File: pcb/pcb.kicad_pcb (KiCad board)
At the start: 6 copper layers, 172 parts, among them J1 mcu_debug, J1201 Conn_02x07_Top_Bottom, J1401 FPGA_JTAG, J301 Conn_02x05_Top_Bottom, J302 1658525-9, J601 DB15_Female_HighDensity, U201 TPS54325PWPR, U202 TPS54294PWP, U301 BGA112, U401 COM-09032, U666 XC7A75T-FTG256, U701 AS7C316098A-10TIN, Y1101 ECS-2520MV-080-BN-TR, Y301 Crystal_GND24

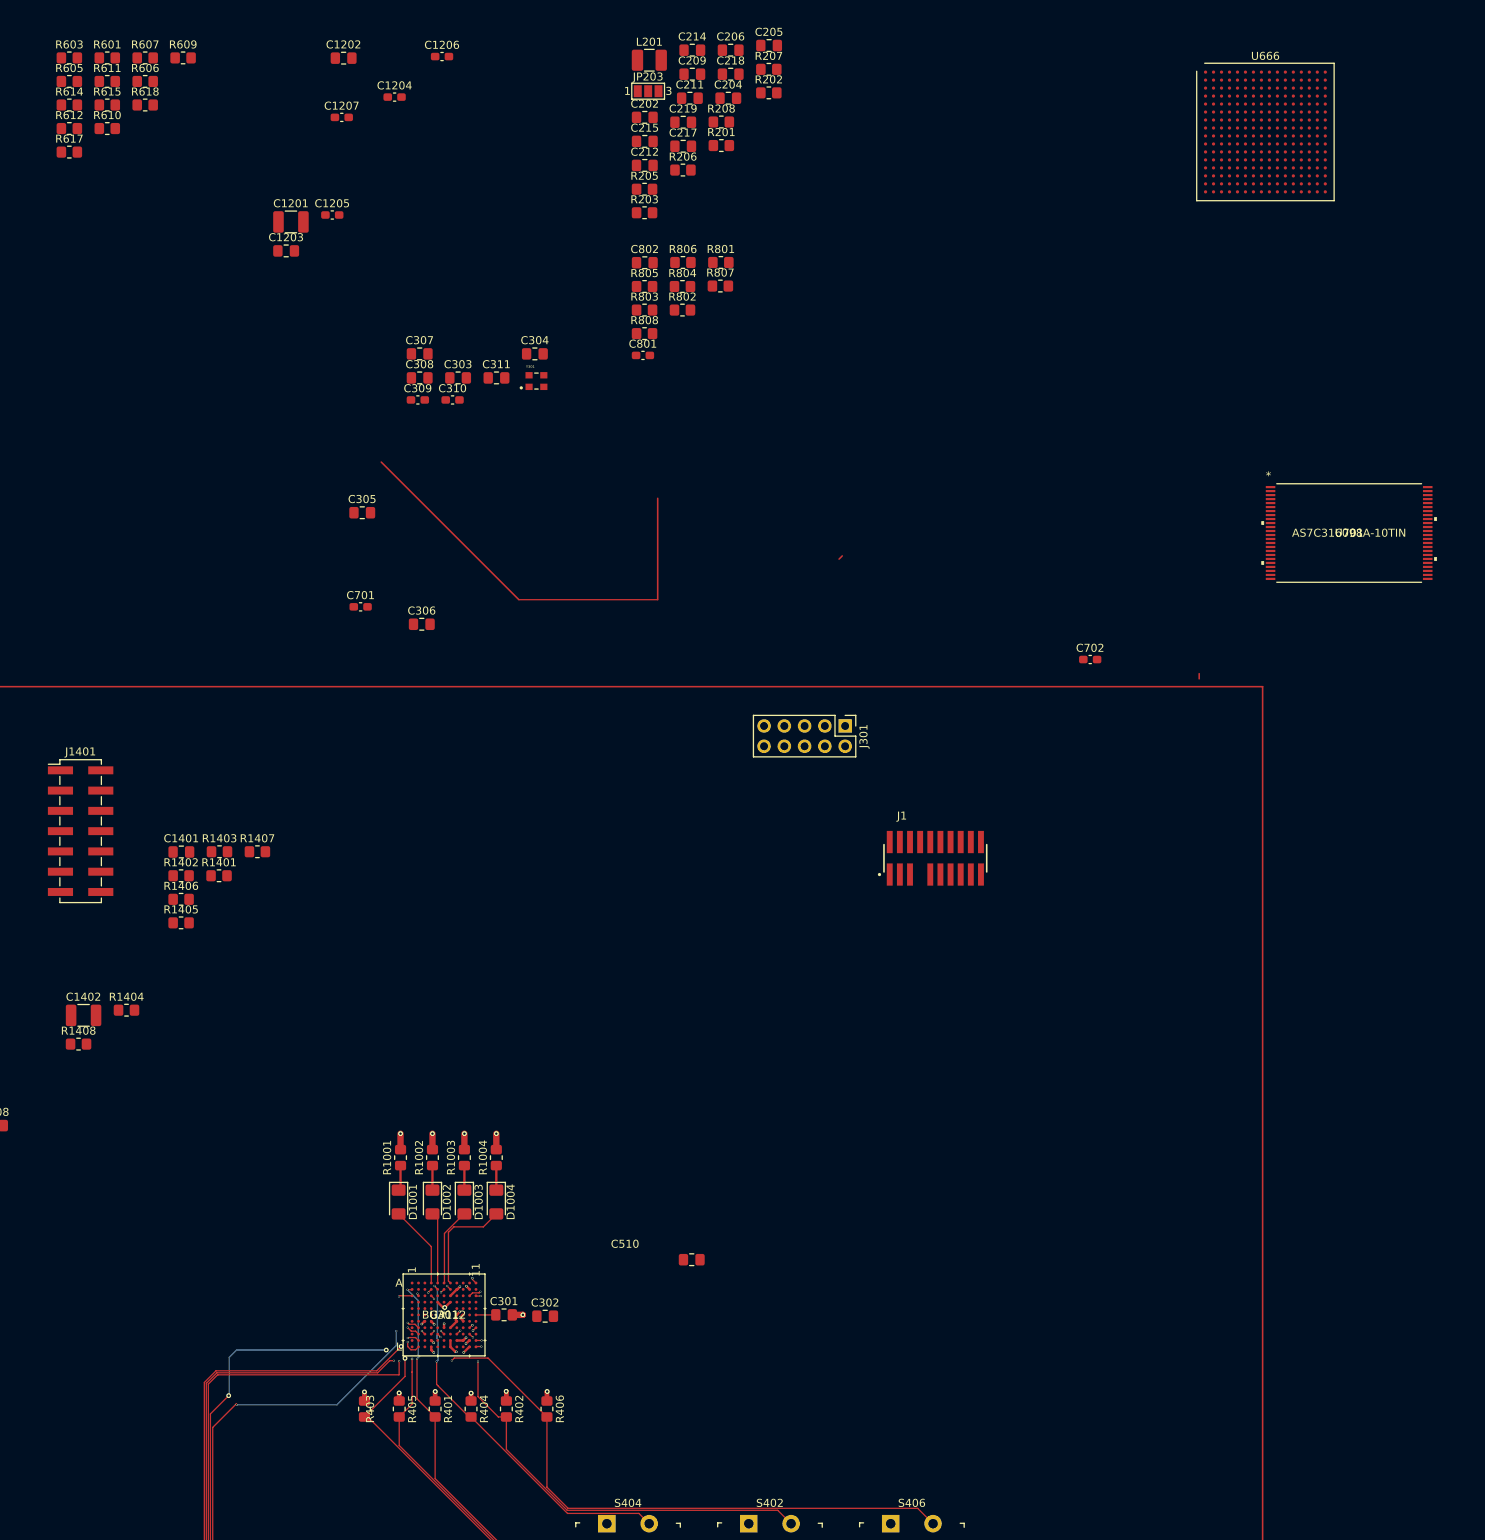
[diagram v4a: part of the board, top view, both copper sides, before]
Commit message: switch some pins for more erqonomiq layout
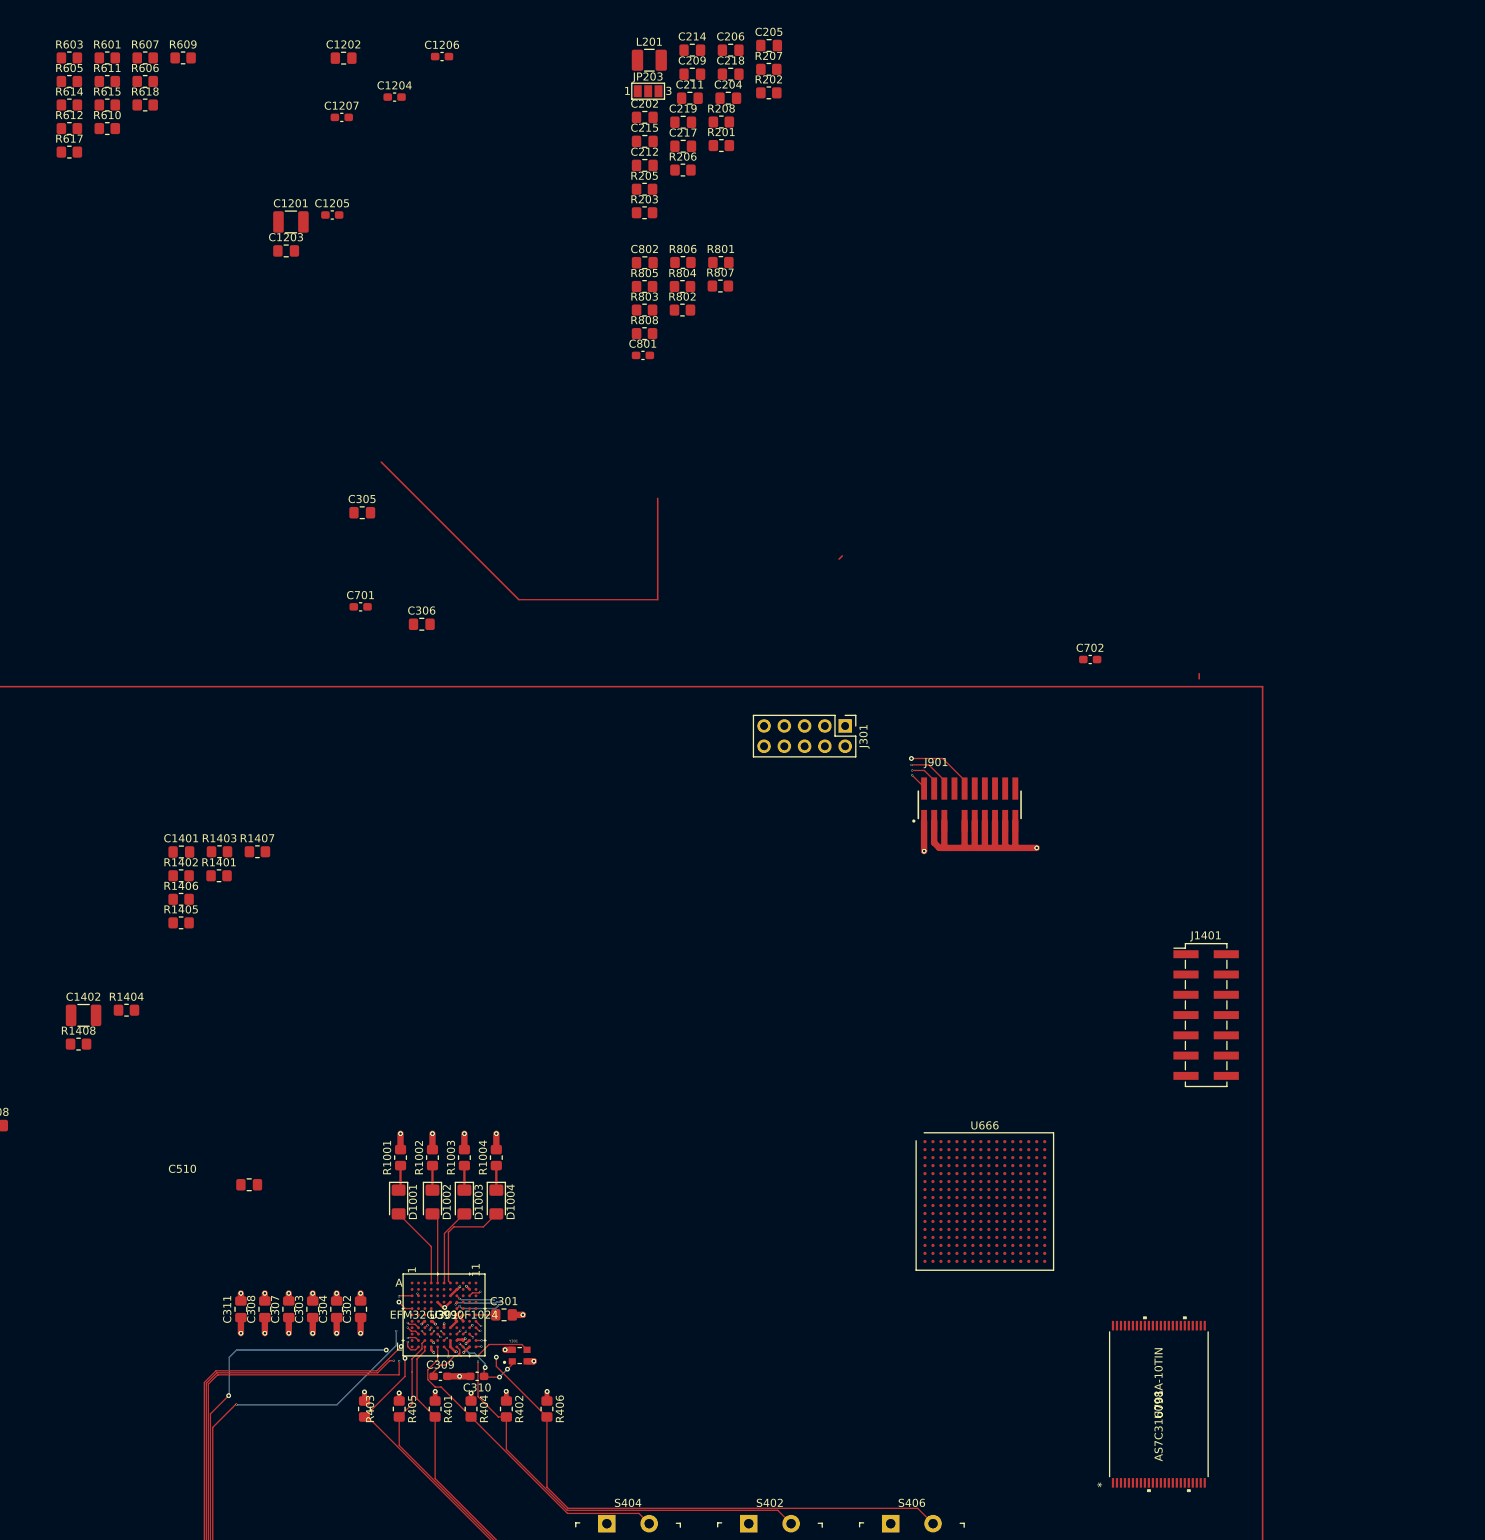
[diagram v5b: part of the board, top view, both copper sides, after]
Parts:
- removed J1: mcu_debug, debug-footprints:SAMTEC_FTSH-110-01-L-DV-007
- added J901: FTSH-110-01-L-DV-007, debug-footprints:SAMTEC_FTSH-110-01-L-DV-007, F.Cu at (233.3, 34.8)
- U301: value BGA112 -> EFM32GG990F1024
- moved J1401 142.9 mm to (262.9, 61.1)
- moved U666 138.5 mm to (235.2, 84.5)
- moved C310 122.4 mm to (171.6, 106.4), turned to 180 degrees
- moved C309 122.4 mm to (167.0, 106.4)
- moved C304 122.2 mm to (154.0, 98.0), turned to 90 degrees
- moved Y301 122.1 mm to (176.9, 103.8)
- moved C311 121.0 mm to (142.0, 98.0), turned to 90 degrees
- moved C307 120.8 mm to (148.0, 98.0), turned to 90 degrees
- moved C308 118.3 mm to (145.0, 98.0), turned to 90 degrees
- moved C303 118.1 mm to (151.0, 98.0), turned to 90 degrees
- moved U701 111.7 mm to (257.0, 109.9), turned to 90 degrees
- moved C510 56.2 mm to (143.0, 82.4)
- moved C302 23.1 mm to (157.0, 98.0), turned to 90 degrees
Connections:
- net POWER_IN renamed +5V
- U301 pad A11: bo_js_button_1 -> unconnected-(U301-PadA11)
- U301 pad B1: bo_button_1 -> unconnected-(U301-PadB1)
- U301 pad B4: bo_button_3 -> unconnected-(U301-PadB4)
- U301 pad B5: bo_button_4 -> unconnected-(U301-PadB5)
- U301 pad B6: bo_button_5 -> unconnected-(U301-PadB6)
- U301 pad B7: bo_button_6 -> unconnected-(U301-PadB7)
- U301 pad C11: bo_button_2 -> unconnected-(U301-PadC11)
- U301 pad C4: /Mcu/MCU_GPIO_4 -> unconnected-(U301-PadC4)
- U301 pad C5: /Mcu/MCU_GPIO_5 -> unconnected-(U301-PadC5)
- U301 pad C6: /Mcu/MCU_GPIO_6 -> unconnected-(U301-PadC6)
- U301 pad E1: /Mcu/MCU_GPIO_7 -> /Mcu/MCU_GPIO_4
- U301 pad E10: /Mcu/MCU_GPIO_12 -> unconnected-(U301-PadE10)
- U301 pad E2: /Mcu/MCU_GPIO_8 -> unconnected-(U301-PadE2)
- U301 pad E3: /Mcu/MCU_GPIO_9 -> unconnected-(U301-PadE3)
- U301 pad E4: /Mcu/MCU_GPIO_10 -> unconnected-(U301-PadE4)
- U301 pad E9: /Mcu/MCU_GPIO_11 -> unconnected-(U301-PadE9)
- U301 pad G11: unconnected-(U301-PadG11) -> bo_button_6
- U301 pad H11: bo_js_hor_1 -> bo_button_2
- U301 pad H3: unconnected-(U301-PadH3) -> js_gpio_5
- U301 pad H4: unconnected-(U301-PadH4) -> bo_button_3
- U301 pad H9: bo_js_hor_2 -> unconnected-(U301-PadH9)
- U301 pad J11: bo_js_vert_2 -> unconnected-(U301-PadJ11)
- U301 pad J7: js_gpio_5 -> unconnected-(U301-PadJ7)
- U301 pad J9: unconnected-(U301-PadJ9) -> bo_js_button_1
- U301 pad K3: unconnected-(U301-PadK3) -> bo_button_5
- U301 pad L3: unconnected-(U301-PadL3) -> bo_button_1
- U301 pad L5: unconnected-(U301-PadL5) -> bo_button_4
- U301 pad L6: unconnected-(U301-PadL6) -> bo_js_hor_1
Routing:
- net mcu_debug_reset: track 0.00 -> 108.9 mm, vias 0 -> 2
- net mcu_debug_serial_out: track 0.00 -> 99.8 mm, vias 0 -> 3
- net mcu_debug_serial_clock: track 0.00 -> 98.9 mm, vias 0 -> 3
- net mcu_debug_serial_data: track 0.00 -> 96.7 mm, vias 0 -> 3
- net GND: track 16.6 -> 66.6 mm, vias 13 -> 23
- net +3.3V: track 15.2 -> 30.9 mm, vias 12 -> 19
- net Net-(C309-Pad1): track 0.00 -> 15.3 mm
- net Net-(C310-Pad1): track 0.00 -> 11.1 mm, vias 0 -> 4
- net bo_button_6: track 84.3 -> 74.8 mm
- net js_gpio_5: track 84.6 -> 93.3 mm, vias 0 -> 1
- net bo_button_1: track 99.1 -> 91.0 mm, vias 2 -> 0
- net bo_button_5: track 84.0 -> 76.1 mm, vias 2 -> 0
- net bo_js_button_1: track 146.8 -> 139.5 mm
- net bo_button_4: track 47.1 -> 40.1 mm, vias 2 -> 0
- net bo_button_3: track 69.1 -> 64.3 mm
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
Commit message: no
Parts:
- moved J1201 228.7 mm to (262.0, 78.3)
- moved R609 139.7 mm to (190.8, 69.2), turned to -90 degrees
- moved R607 137.4 mm to (190.8, 64.4), turned to -90 degrees
- moved R601 135.3 mm to (190.8, 59.6), turned to -90 degrees
- moved R603 133.6 mm to (190.8, 54.9), turned to -90 degrees
- moved R606 133.4 mm to (187.8, 64.4), turned to -90 degrees
- moved R611 131.3 mm to (187.8, 59.6), turned to -90 degrees
- moved R605 129.6 mm to (187.8, 54.9), turned to -90 degrees
- moved R618 129.5 mm to (184.9, 64.4), turned to -90 degrees
- moved R615 127.3 mm to (184.9, 59.6), turned to -90 degrees
- moved R614 125.5 mm to (184.9, 54.9), turned to -90 degrees
- moved J601 124.8 mm to (179.8, 31.2), turned to 0 degrees
- moved R610 123.4 mm to (181.9, 59.6), turned to -90 degrees
- moved R612 121.5 mm to (181.9, 54.9), turned to -90 degrees
- moved R617 117.5 mm to (179.0, 54.9), turned to -90 degrees
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
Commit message: workon
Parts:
- added J201: USB_B_Mini, usb:USB2066-05-RBHM-15-STB-00-00-A, F.Cu at (52.9, 79.3)
- added J801: 10067847-001RLF, sd:10067847-001RLF, F.Cu at (263.5, 35.0)
- added U1402: S25FL127SABMFV101, flash:S25FL127SABMFV101, F.Cu at (190.8, 158.7)
- moved R613 265.2 mm to (182.8, 62.1), turned to -90 degrees
- moved R602 245.9 mm to (154.2, 62.1), turned to 90 degrees
- moved C202 139.7 mm to (102.8, 55.6)
- moved C204 139.7 mm to (113.2, 53.2)
- moved C205 139.7 mm to (118.3, 46.6)
- moved C206 139.7 mm to (113.5, 47.2)
- moved C209 139.7 mm to (108.7, 50.2)
- moved C211 139.7 mm to (108.4, 53.2)
- moved C212 139.7 mm to (102.8, 61.6)
- moved C214 139.7 mm to (108.7, 47.2)
- moved C215 139.7 mm to (102.8, 58.6)
- moved C217 139.7 mm to (107.6, 59.2)
- moved C218 139.7 mm to (113.5, 50.2)
- moved C219 139.7 mm to (107.6, 56.2)
- moved JP203 139.7 mm to (103.2, 52.3)
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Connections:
- U666 pad B4: unconnected-(U666-PadB4) -> FGPA_MCU_SPI_CLK
- U666 pad E6: FGPA_MCU_SPI_CLK -> unconnected-(U666-PadE6)
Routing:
- net FGPA_MCU_SPI_CS: track 0.00 -> 88.2 mm, vias 0 -> 3
- net FGPA_MCU_SPI_CLK: track 0.00 -> 85.7 mm, vias 0 -> 3
- net FGPA_MCU_SPI_SDI: track 0.00 -> 85.5 mm, vias 0 -> 3
- net FGPA_MCU_SPI_SDO: track 0.00 -> 82.9 mm, vias 0 -> 3
- net MCU_DEBUG_US0_CS: track 167.9 -> 113.6 mm
- net bo_button_3: track 64.3 -> 99.3 mm
- net bo_button_5: track 76.1 -> 110.9 mm
- net bo_button_4: track 40.1 -> 74.8 mm
- net bo_button_6: track 74.8 -> 109.4 mm
- net bo_button_1: track 91.0 -> 125.7 mm
- net bo_button_2: track 57.3 -> 91.9 mm
- net MCU_DEBUG_US0_MOSI: track 109.4 -> 108.4 mm

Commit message: psu wiring and power cables
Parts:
- added R606: 17400, Resistor_SMD:R_0603_1608Metric_Pad0.98x0.95mm_HandSolder, F.Cu at (271.8, -33.0)
- added R607: 8760, Resistor_SMD:R_0603_1608Metric_Pad0.98x0.95mm_HandSolder, F.Cu at (271.8, -30.5)
- added R608: 4420, Resistor_SMD:R_0603_1608Metric_Pad0.98x0.95mm_HandSolder, F.Cu at (267.4, -33.0)
- added R609: 2200, Resistor_SMD:R_0603_1608Metric_Pad0.98x0.95mm_HandSolder, F.Cu at (280.5, -33.0)
- added R610: 1300, Resistor_SMD:R_0603_1608Metric_Pad0.98x0.95mm_HandSolder, F.Cu at (271.8, -35.5)
- added R611: 550, Resistor_SMD:R_0603_1608Metric_Pad0.98x0.95mm_HandSolder, F.Cu at (267.4, -30.5)
- added R612: 8760, Resistor_SMD:R_0603_1608Metric_Pad0.98x0.95mm_HandSolder, F.Cu at (276.1, -35.5)
- added R613: 4420, Resistor_SMD:R_0603_1608Metric_Pad0.98x0.95mm_HandSolder, F.Cu at (276.1, -33.0)
- added R614: 2200, Resistor_SMD:R_0603_1608Metric_Pad0.98x0.95mm_HandSolder, F.Cu at (280.5, -35.5)
- added R615: 1300, Resistor_SMD:R_0603_1608Metric_Pad0.98x0.95mm_HandSolder, F.Cu at (267.4, -35.5)
- added R616: 550, Resistor_SMD:R_0603_1608Metric_Pad0.98x0.95mm_HandSolder, F.Cu at (276.1, -30.5)
- JP201, JP202, JP203: footprint Jumper:SolderJumper-3_P1.3mm_Open_Pad1.0x1.5mm_NumberLabels -> Jumper:SolderJumper-2_P1.3mm_Open_Pad1.0x1.5mm
- moved C506 299.6 mm to (354.8, 96.6)
- moved C513 290.6 mm to (351.8, 84.8)
- moved C516 290.6 mm to (346.9, 98.4)
- moved C517 290.6 mm to (361.4, 84.4)
- moved C518 290.6 mm to (356.6, 84.4)
- moved R501 290.6 mm to (360.2, 87.4)
- moved R502 290.6 mm to (349.4, 101.0)
- moved R504 290.6 mm to (360.2, 90.3)
- moved C503 290.6 mm to (344.6, 92.4)
- moved C505 290.6 mm to (354.2, 92.0)
- moved C507 290.6 mm to (355.4, 87.8)
- moved C509 290.6 mm to (349.4, 92.0)
- moved C520 290.6 mm to (345.8, 89.0)
- moved C522 290.6 mm to (350.6, 89.0)
- moved C523 290.6 mm to (349.4, 98.1)
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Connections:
- C1102 pad 1: +3V3 -> +3.3V
- C1103 pad 1: +3V3 -> +3.3V
- C1104 pad 1: +3V3 -> +3.3V
- C1105 pad 1: +3V3 -> +3.3V
- C1106 pad 1: +3V3 -> +3.3V
- C1107 pad 1: +3V3 -> +3.3V
- C1108 pad 1: +3V3 -> +3.3V
- C1109 pad 1: +3V3 -> +3.3V
- C1110 pad 1: +3V3 -> +3.3V
- C1111 pad 1: +3V3 -> +3.3V
- C1112 pad 1: +3V3 -> +3.3V
- C1113 pad 1: +3V3 -> +3.3V
- C1114 pad 1: +3V3 -> +3.3V
- C1115 pad 1: +3V3 -> +3.3V
- JP203 pad 2: +3V3 -> +3.3V
- U401 pad B2A: GND -> bo_js_button_1
- U401 pad S1: bo_js_button_1 -> unconnected-(U401-PadS1)
- U401 pad S2: bo_js_button_1 -> unconnected-(U401-PadS1)
- U401 pad S3: bo_js_button_1 -> unconnected-(U401-PadS1)
- U401 pad S4: bo_js_button_1 -> unconnected-(U401-PadS1)
- U666 pad A16: +3V3 -> +3.3V
- U666 pad B13: +3V3 -> +3.3V
- U666 pad C10: +3V3 -> +3.3V
- U666 pad E14: +3V3 -> +3.3V
- U666 pad H15: +3V3 -> +3.3V
- U666 pad J12: +3V3 -> +3.3V
- U666 pad L16: +3V3 -> +3.3V
- U666 pad M13: +3V3 -> +3.3V
- U666 pad N10: +3V3 -> +3.3V
- U666 pad P7: +3V3 -> +3.3V
- U666 pad R14: +3V3 -> +3.3V
- U666 pad T11: +3V3 -> +3.3V
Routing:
- net +1V8: track 0.00 -> 202.5 mm, vias 0 -> 6
- net +1V0: track 0.00 -> 196.2 mm, vias 0 -> 7
- net unconnected-(U401-PadS1): track 0.00 -> 139.5 mm, vias 0 -> 1
- net bo_js_button_1: track 139.5 -> 0.00 mm, vias 1 -> 0
- net GND: track 66.6 -> 139.9 mm, vias 23 -> 41
- net Net-(R205-Pad1): track 0.00 -> 44.2 mm, vias 0 -> 5
- net Net-(C216-Pad1): track 0.00 -> 43.8 mm, vias 0 -> 2
- net +5V: track 0.00 -> 30.2 mm, vias 0 -> 12
- net Net-(C210-Pad1): track 0.00 -> 27.4 mm, vias 0 -> 2
- net Net-(R201-Pad2): track 0.00 -> 23.2 mm, vias 0 -> 2
- net Net-(C218-Pad1): track 0.00 -> 19.3 mm
- net Net-(C201-Pad1): track 0.00 -> 18.6 mm
- net Net-(R206-Pad2): track 0.00 -> 18.4 mm, vias 0 -> 3
- net Net-(C211-Pad1): track 0.00 -> 14.4 mm, vias 0 -> 2
- net Net-(C209-Pad2): track 0.00 -> 12.2 mm
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- added copper zone on In2.Cu, net +1V0
- added copper zone on In3.Cu, net +1V0
- added copper zone on In2.Cu, net +1V8
- added copper zone on In1.Cu, net +5V
- added copper zone on F.Cu, net GND
